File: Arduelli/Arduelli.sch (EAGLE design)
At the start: 94 parts, among them J1 47346-0001, J2 DF12-ELLI-RECEPTABLE-BOTTOM, J4 FTDI-SER-6-PP, J5 JTAG_PROG, J6 47346-0001, Q1 NTZD3152P, Q2 2N7002PT, Q3 MOSFET-PCHANNELIRLML2244, U1 ARDUINO_SHIELDLONGPADS, U2 STM32F103RBT, U3 ADUM4160BRWZ, U4 ADUM4160BRWZ, U5 NCP1117, X1 M-BOLT-2, X2 M-BOLT-2, X3 M-BOLT-2, X4 M-BOLT-2, X5 M-BOLT-2, Y1 8MHz

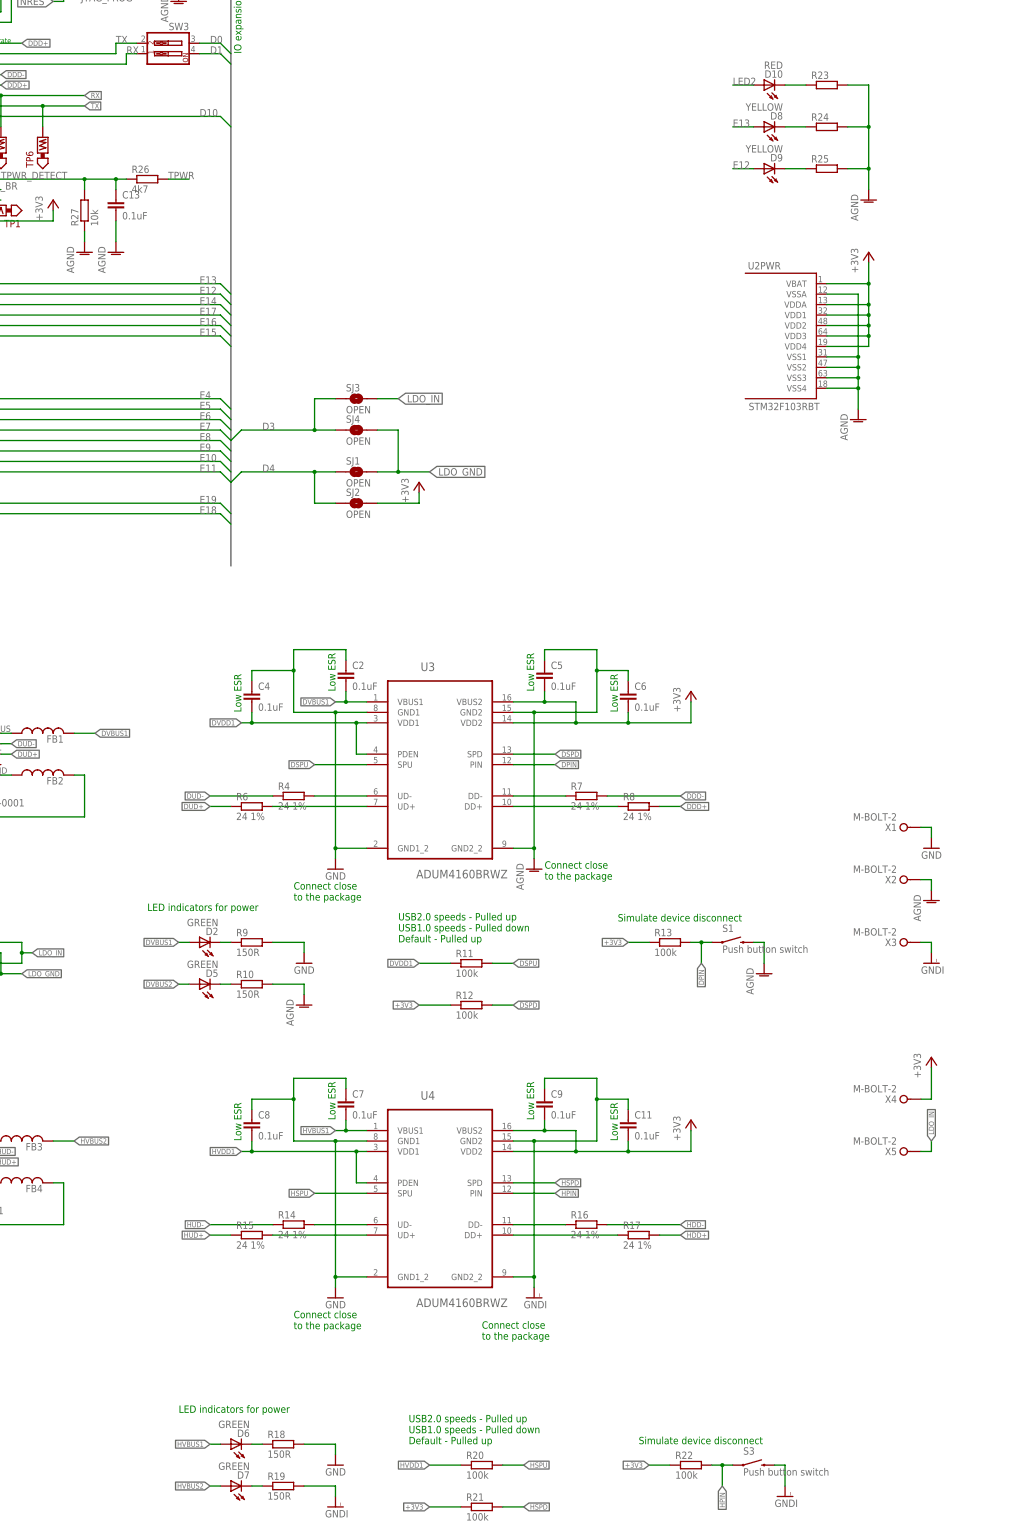
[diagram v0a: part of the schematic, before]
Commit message: Fixes to Schematic for connec. problems in layout
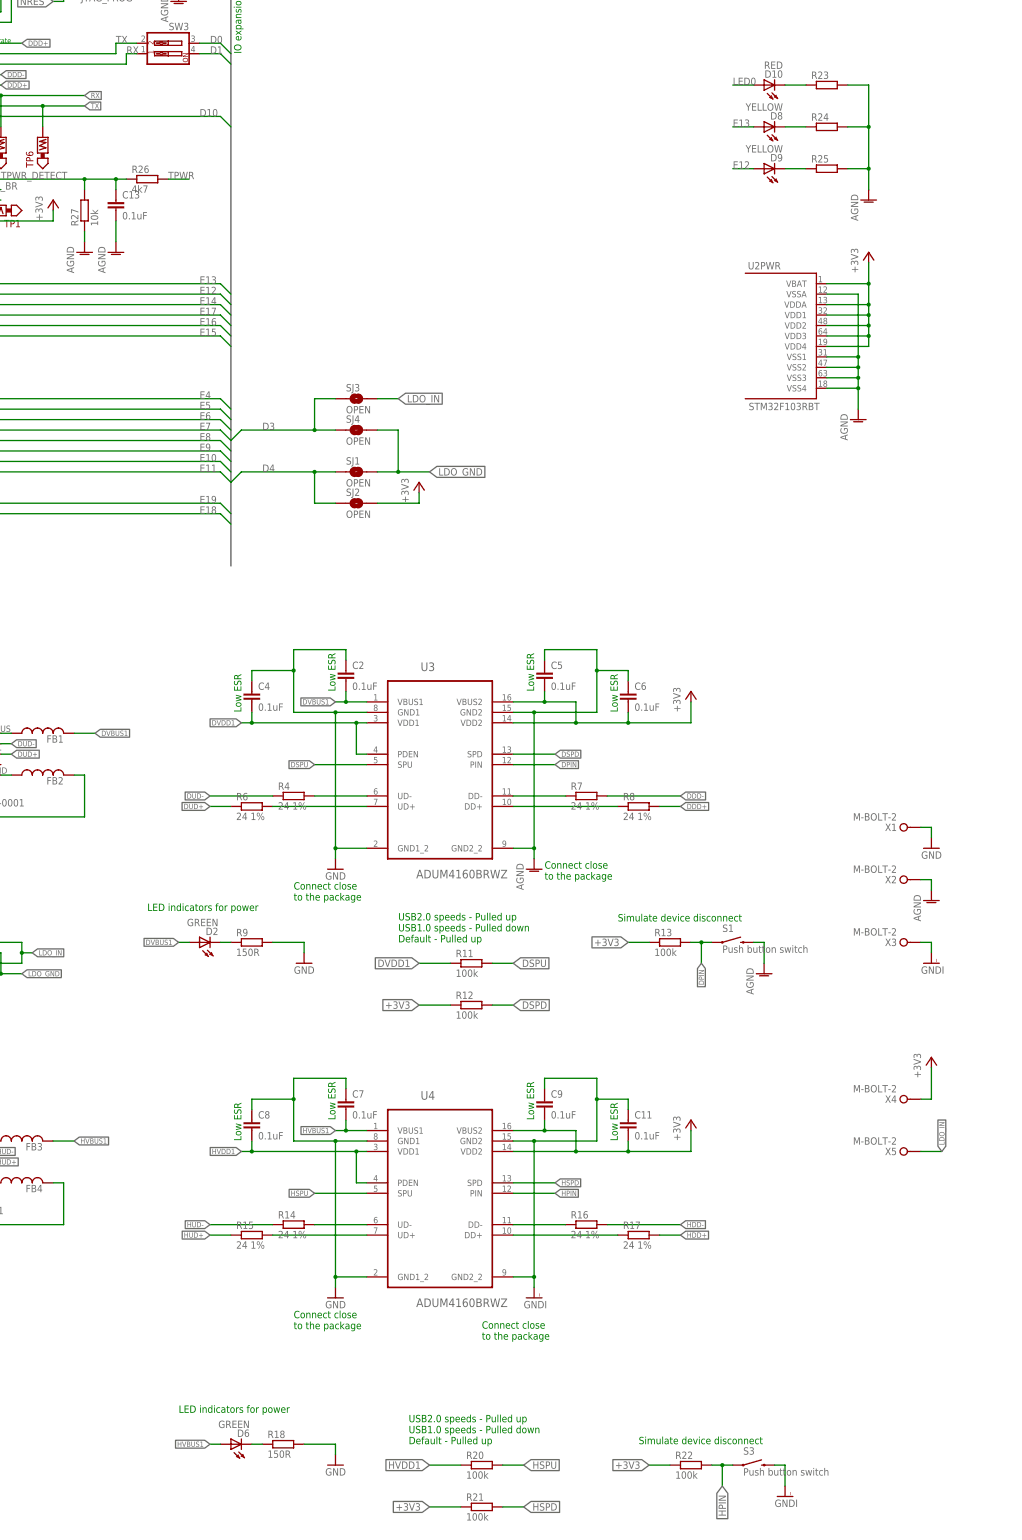
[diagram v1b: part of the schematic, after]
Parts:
- removed D5, D7: GREEN, SparkFun-LED:LED-GREEN0603
- removed R10, R19: 150R, ELL-i-Passives:R0402
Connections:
- removed net DVBUS2: D5.A
- removed net LED2: D10.A
- removed net N$12: D5.C, R10.1
- removed net N$18: R11.1
- removed net N$19: R12.1
- removed net N$20: R11.2
- removed net N$21: R12.2
- removed net N$22: R13.1
- removed net N$32: R20.1
- removed net N$33: R21.1
- removed net N$34: R20.2
- removed net N$35: X5.KL1
- removed net N$37: R21.2
- removed net N$39: R22.1
- removed net N$40: R22.2, S3.1
- removed net N$5: D7.C, R19.1
- net +3V3: now also R12.1, R13.1, R21.1, R22.1
- net AGND: no longer R10.2
- net DSPD: now also R12.2
- net DSPU: now also R11.2
- net DVDD1: now also R11.1
- net GNDI: no longer R19.2
- net HPIN: now also R22.2, S3.1
- net HSPD: now also R21.2
- net HSPU: now also R20.2
- net HVBUS1: now also FB3.1
- net HVBUS2: no longer D7.A, FB3.1
- net HVDD1: now also R20.1
- net LDO_IN: now also X5.KL1
- net LED0: now also D10.A

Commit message: Proper naming of supply nets to represent multiple voltage symbols
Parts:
- added SJ5, SJ8: OPEN, SparkFun-Passives:SOLDERJUMPERNO
- added SJ6, SJ7: CLOSED, SparkFun-Passives:SOLDERJUMPERNO
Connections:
- removed net +5V0: C16.+, TP2.P$1, U5.OUT, U5.TAB
- removed net N$23: R13.2, S1.1
- new net ARDUELLI-3V3: C1.1, Q1.S1, Q1.S2, R2.2, U2PWR.VBAT, U2PWR.VDD1, U2PWR.VDD2, U2PWR.VDD3, U2PWR.VDD4, U2PWR.VDDA
- new net POE-3V3: D3.A, Q1.G1, Q2.G, R3.2
- new net USB-3V3: C16.+, Q1.D1, R1.2, TP2.P$1, U5.OUT, U5.TAB
- net +3V3: no longer C1.1, D3.A, Q1.D1, Q1.G1, Q1.S1, Q1.S2, Q2.G, R1.2, R2.2, R3.2, U2PWR.VBAT, U2PWR.VDD1, U2PWR.VDD2, U2PWR.VDD3, U2PWR.VDD4, U2PWR.VDDA
- net DDD+: now also SJ7.1, SJ7.2, SJ8.1
- net DDD-: now also SJ5.1, SJ6.1, SJ6.2
- net DPIN: now also R13.2, S1.1
- net HDD+: now also SJ8.2
- net HDD-: now also SJ5.2

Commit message: Changed the values of the capacitor on NCP1117
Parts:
- C39: value 100nF -> 10uF
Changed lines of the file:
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@@
 <part name="C16" library="ELL-i-Passives" deviceset="CPOL" device="6032" value="47u"/>
 <part name="C17" library="ELL-i-Passives" deviceset="C" device="0805" value="47pF"/>
-<part name="C39" library="ELL-i-Passives" deviceset="C" device="0805" value="100nF"/>
+<part name="C39" library="ELL-i-Passives" deviceset="C" device="0805" value="10uF"/>
 <part name="TP2" library="ELL-i-Passives" deviceset="TEST_POINT" device="-5021"/>
 <part name="TP3" library="ELL-i-Passives" deviceset="TEST_POINT" device="-5021"/>
